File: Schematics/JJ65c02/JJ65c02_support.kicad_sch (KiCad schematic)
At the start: 31 parts, among them SW2 SW_SPDT, U1 74HC00, U2 TXB0108PWR, U3 TXB0104PW, U4 74LS573, U5 TLV2217-33KCSE3, X2 1.8Mhz

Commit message: More work on rp2040-version2
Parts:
- U3: footprint Package_SO:SOIC-14_3.9x8.7mm_P1.27mm -> Package_SO:TSSOP-14_4.4x5mm_P0.65mm
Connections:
- net CLK: now also DECODER1.10 (IN10); no longer DECODER1.1 (CLK/IN1)
- net GND: now also USBC1.B12 (GND)
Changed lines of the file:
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@@
 	)
 	(junction
-		(at 222.25 44.45)
-		(diameter 0)
-		(color 0 0 0 0)
-	)
-	(junction
 		(at 200.66 76.2)
 		(diameter 0)
@@
 		(color 0 0 0 0)
 	)
+	(junction
+		(at 212.09 54.61)
+		(diameter 0)
+		(color 0 0 0 0)
+	)
 	(no_connect
 		(at 39.37 30.48)
@@
 	)
 	(no_connect
+		(at 173.99 76.2)
+	)
+	(no_connect
 		(at 39.37 43.18)
 	)
@@
 	)
 	(no_connect
-		(at 173.99 99.06)
-	)
-	(no_connect
 		(at 234.95 31.75)
 	)
@@
 	(wire
 		(pts
-			(xy 172.72 73.66) (xy 172.72 76.2)
-		)
-		(stroke
-			(width 0)
-			(type default)
-		)
-	)
-	(wire
-		(pts
 			(xy 38.1 185.42) (xy 39.37 185.42)
 		)
@@
 	(wire
 		(pts
+			(xy 212.09 54.61) (xy 222.25 54.61)
+		)
+		(stroke
+			(width 0)
+			(type default)
+		)
+	)
+	(wire
+		(pts
 			(xy 153.67 46.99) (xy 162.56 46.99)
 		)
@@
 	(wire
 		(pts
+			(xy 222.25 44.45) (xy 222.25 54.61)
+		)
+		(stroke
+			(width 0)
+			(type default)
+		)
+	)
+	(wire
+		(pts
 			(xy 232.41 77.47) (xy 229.87 77.47)
 		)
@@
 	(wire
 		(pts
+			(xy 207.01 54.61) (xy 212.09 54.61)
+		)
+		(stroke
+			(width 0)
+			(type default)
+		)
+	)
+	(wire
+		(pts
 			(xy 250.19 72.39) (xy 250.19 74.93)
 		)
@@
 		)
 	)
-	(bus
+	(wire
 		(pts
-			(xy 166.37 76.2) (xy 166.37 78.74)
+			(xy 171.45 99.06) (xy 173.99 99.06)
 		)
 		(stroke
@@
 		)
 	)
-	(wire
+	(bus
 		(pts
-			(xy 171.45 91.44) (xy 173.99 91.44)
+			(xy 166.37 76.2) (xy 166.37 78.74)
 		)
 		(stroke
@@
 	(wire
 		(pts
-			(xy 199.39 99.06) (xy 201.93 99.06)
+			(xy 171.45 91.44) (xy 173.99 91.44)
 		)
 		(stroke
@@
 	(wire
 		(pts
-			(xy 222.25 40.64) (xy 222.25 44.45)
+			(xy 199.39 99.06) (xy 201.93 99.06)
 		)
 		(stroke
@@
 	(wire
 		(pts
-			(xy 171.45 73.66) (xy 172.72 73.66)
-		)
-		(stroke
-			(width 0)
-			(type default)
-		)
-	)
-	(wire
-		(pts
 			(xy 34.29 33.02) (xy 34.29 41.91)
 		)
@@
 	(wire
 		(pts
-			(xy 172.72 76.2) (xy 173.99 76.2)
-		)
-		(stroke
-			(width 0)
-			(type default)
-		)
-	)
-	(wire
-		(pts
 			(xy 157.48 137.16) (xy 157.48 148.59)
 		)
@@
 	(global_label "CLK"
 		(shape input)
-		(at 171.45 73.66 180)
+		(at 171.45 99.06 180)
 		(fields_autoplaced yes)
 		(effects
@@
 		)
 		(property "Intersheetrefs" "${INTERSHEET_REFS}"
-			(at 165.9051 73.66 0)
+			(at 165.9051 99.06 0)
 			(effects
 				(font
@@
 			)
 		)
-		(property "Description" ""
+		(property "Description" "Crystal Clock Oscillator, DIP14-style metal package"
 			(at 120.65 36.83 0)
 			(effects
@@
 			)
 		)
-		(property "Description" ""
+		(property "Description" "Light emitting diode"
 			(at 162.56 40.64 0)
 			(effects
@@
 			)
 		)
-		(property "Description" ""
+		(property "Description" "Resistor"
 			(at 162.56 33.02 0)
 			(effects
@@
 			)
 		)
-		(property "Description" ""
+		(property "Description" "Unpolarized capacitor"
 			(at 125.73 144.78 0)
 			(effects
@@
 			)
 		)
-		(property "Description" ""
+		(property "Description" "Resistor"
 			(at 135.89 144.78 0)
 			(effects
@@
 			)
 		)
-		(property "Description" ""
+		(property "Description" "quad 2-input NAND gate"
 			(at 242.57 74.93 0)
 			(effects
@@
 			)
 		)
-		(property "Description" ""
+		(property "Description" "Resistor"
 			(at 232.41 83.82 0)
 			(effects
@@
 			)
 		)
-		(property "Description" ""
+		(property "Description" "Resistor"
 			(at 24.13 48.26 0)
 			(effects
@@
 			)
 		)
-		(property "Description" ""
+		(property "Description" "Switch, single pole double throw"
 			(at 229.87 29.21 0)
 			(effects
@@
 			)
 		)
-		(property "Description" ""
+		(property "Description" "Resistor"
 			(at 152.4 144.78 0)
 			(effects
@@
 			)
 		)
-		(property "Footprint" "Package_SO:SOIC-14_3.9x8.7mm_P1.27mm"
+		(property "Footprint" "Package_SO:TSSOP-14_4.4x5mm_P0.65mm"
 			(at 124.46 109.22 0)
 			(effects
@@
 			)
 		)
-		(property "Description" ""
+		(property "Description" "4-Bit Bidirectional Voltage-Level Translator, Auto Direction Sensing and ±15-kV ESD Protection, 1.2 - 3.6V APort, 1.65 - 5.5V BPort, TSSOP-14"
 			(at 124.46 90.17 0)
 			(effects
@@
 			)
 		)
-		(property "Description" ""
+		(property "Description" "Audio Jack, 3 Poles (Stereo / TRS)"
 			(at 162.56 151.13 0)
 			(effects
@@
 			)
 		)
-		(property "Description" ""
+		(property "Description" "Resistor"
 			(at 26.67 27.94 0)
 			(effects
@@
 			)
 		)
-		(property "Description" ""
+		(property "Description" "Unpolarized capacitor"
 			(at 72.39 125.73 0)
 			(effects
@@
 			)
 		)
-		(property "Description" ""
+		(property "Description" "6-pin Mini-DIN connector"
 			(at 81.28 54.61 0)
 			(effects
@@
 			)
 		)
-		(property "Description" ""
+		(property "Description" "Polarized capacitor"
 			(at 262.89 39.37 0)
 			(effects
@@
 			)
 		)
-		(property "Description" ""
+		(property "Description" "15-pin female receptacle socket D-SUB connector, High density (3 columns), Triple Row, Generic, VGA-connector"
 			(at 46.99 38.1 0)
 			(effects
@@
 			)
 		)
-		(property "Description" ""
+		(property "Description" "Unpolarized capacitor"
 			(at 196.85 64.77 0)
 			(effects
@@
 			)
 		)
-		(property "Description" ""
+		(property "Description" "Unpolarized capacitor"
 			(at 143.51 153.67 0)
 			(effects
@@
 			)
 		)
-		(property "Description" ""
+		(property "Description" "Resistor"
 			(at 34.29 48.26 0)
 			(effects
@@
 			)
 		)
-		(property "Description" ""
+		(property "Description" "Resistor"
 			(at 29.21 48.26 0)
 			(effects
@@
 			)
 		)
-		(property "Description" ""
+		(property "Description" "Resistor"
 			(at 26.67 38.1 0)
 			(effects
@@
 			)
 		)
-		(property "Description" ""
+		(property "Description" "quad 2-input NAND gate"
 			(at 257.81 74.93 0)
 			(effects
@@
 			)
 		)
-		(property "Description" ""
+		(property "Description" "Resistor"
 			(at 119.38 153.67 0)
 			(effects
@@
 			)
 		)
-		(property "Description" ""
+		(property "Description" "USB Power-Only 6P Type-C Receptacle connector"
 			(at 207.01 36.83 0)
 			(effects
@@
 		(pin "1"
 		)
-		(pin "2"
-		)
 		(pin "3"
 		)
 		(pin "4"
 		)
+		(pin "B12"
+		)
+		(pin "1"
+		)
+		(pin "2"
+		)
 		(instances
 			(project "JJ65c02"
@@
 			)
 		)
-		(property "Description" ""
+		(property "Description" "8-bit Latch 3-state outputs"
 			(at 220.98 133.35 0)
 			(effects
@@
 			)
 		)
-		(property "Description" ""
+		(property "Description" "Resistor"
 			(at 26.67 33.02 0)
 			(effects
@@
 			)
 		)
-		(property "Description" ""
+		(property "Description" "50mA Ultra-Low Quiescent Current LDO Voltage Regulator, 3.3V fixed output, TO-252/SOT-223"
 			(at 250.19 33.02 0)
 			(effects

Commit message: Latest Kicad schematics and PCB
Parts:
- removed R1: 4.7K, Resistor_THT:R_Axial_DIN0207_L6.3mm_D2.5mm_P7.62mm_Horizontal, symbol Device:R
- removed R11, R13, R14: 470, Resistor_THT:R_Axial_DIN0207_L6.3mm_D2.5mm_P7.62mm_Horizontal, symbol Device:R
- removed R15, R16, R17: 1k, Resistor_THT:R_Axial_DIN0207_L6.3mm_D2.5mm_P7.62mm_Horizontal, symbol Device:R
- added RN2: 4.7k, Resistor_THT:R_Array_SIP6, symbol Device:R_Pack03_SIP_Split
- added RN3: 1k, Resistor_THT:R_Array_SIP6, symbol Device:R_Pack03_SIP_Split
- added RN4: 470, Resistor_THT:R_Array_SIP6, symbol Device:R_Pack03_SIP_Split
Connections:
- net +5V: now also RN2.5 (R3.1)
- net A~{IRQ}: now also RN2.6 (R3.2)
- net BLUE: now also RN4.5 (R3.1)
- net BRIGHT: now also RN3.1 (R1.1), RN3.3 (R2.1), RN3.5 (R3.1)
- net GND: no longer USBC1.B12 (GND)
- net GREEN: now also RN4.3 (R2.1)
- net RED: now also RN4.1 (R1.1)
- net at VGA1.1: now also RN3.2 (R1.2), RN4.2 (R1.2)
- net at VGA1.2: now also RN3.4 (R2.2), RN4.4 (R2.2)
- net at VGA1.3: now also RN3.6 (R3.2), RN4.6 (R3.2)

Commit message: More work on rp2040 updates
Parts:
- U3: footprint Package_SO:TSSOP-14_4.4x5mm_P0.65mm -> Package_SO:SOIC-14_3.9x8.7mm_P1.27mm
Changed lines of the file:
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@@
 			)
 		)
-		(property "Footprint" "Package_SO:TSSOP-14_4.4x5mm_P0.65mm"
+		(property "Footprint" "Package_SO:SOIC-14_3.9x8.7mm_P1.27mm"
 			(at 124.46 109.22 0)
 			(effects

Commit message: Latest versions
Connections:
- net CLK: now also DECODER1.1 (CLK/IN1)
- no-connect marks 35 -> 34
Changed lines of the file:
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@@
 (kicad_sch
-	(version 20231120)
+	(version 20250114)
 	(generator "eeschema")
-	(generator_version "8.0")
+	(generator_version "9.0")
 	(paper "A4")
 	(title_block
@@
 		(comment 4 "Support Circuits")
 	)
+	(text "Support Schematics"
+		(exclude_from_sim no)
+		(at 132.08 17.78 0)
+		(effects
+			(font
+				(size 2.4892 2.4892)
+			)
+			(justify left bottom)
+		)
+	)
+	(text "~{IRQ} Logic Glue"
+		(exclude_from_sim no)
+		(at 240.03 87.63 0)
+		(effects
+			(font
+				(size 2.4892 2.4892)
+			)
+			(justify left bottom)
+		)
+	)
 	(junction
 		(at 262.89 33.02)
@@
 	)
 	(no_connect
-		(at 173.99 76.2)
-	)
-	(no_connect
 		(at 39.37 43.18)
 	)
@@
 	(wire
 		(pts
+			(xy 173.99 73.66) (xy 172.72 73.66)
+		)
+		(stroke
+			(width 0)
+			(type default)
+		)
+	)
+	(wire
+		(pts
 			(xy 234.95 72.39) (xy 229.87 72.39)
 		)
@@
 		)
 	)
+	(wire
+		(pts
+			(xy 173.99 76.2) (xy 173.99 73.66)
+		)
+		(stroke
+			(width 0)
+			(type default)
+		)
+	)
 	(bus
 		(pts
@@
 		)
 	)
-	(text "Support Schematics"
-		(exclude_from_sim no)
-		(at 132.08 17.78 0)
-		(effects
-			(font
-				(size 2.4892 2.4892)
-			)
-			(justify left bottom)
-		)
-	)
-	(text "~{IRQ} Logic Glue"
-		(exclude_from_sim no)
-		(at 240.03 87.63 0)
-		(effects
-			(font
-				(size 2.4892 2.4892)
-			)
-			(justify left bottom)
-		)
-	)
 	(label "a11"
 		(at 172.72 88.9 180)
-		(fields_autoplaced yes)
 		(effects
 			(font
@@
 	(label "pa3v0"
 		(at 33.02 134.62 0)
-		(fields_autoplaced yes)
 		(effects
 			(font
@@
 	(label "d0"
 		(at 204.47 120.65 0)
-		(fields_autoplaced yes)
 		(effects
 			(font
@@
 	(label "pa3v2"
 		(at 33.02 88.9 0)
-		(fields_autoplaced yes)
 		(effects
 			(font
@@
 	(label "pa3v6"
 		(at 33.02 99.06 0)
-		(fields_autoplaced yes)
 		(effects
 			(font
@@
 	(label "d1"
 		(at 204.47 123.19 0)
-		(fields_autoplaced yes)
 		(effects
 			(font
@@
 	(label "d3v4"
 		(at 238.76 130.81 180)
-		(fields_autoplaced yes)
 		(effects
 			(font
@@
 	(label "pa3v1"
 		(at 33.02 86.36 0)
-		(fields_autoplaced yes)
 		(effects
 			(font
@@
 	(label "d4"
 		(at 204.47 130.81 0)
-		(fields_autoplaced yes)
 		(effects
 			(font
@@
 	(label "pa3v6"
 		(at 33.02 154.94 0)
-		(fields_autoplaced yes)
 		(effects
 			(font
@@
 	(label "pa3v5"
 		(at 33.02 96.52 0)
-		(fields_autoplaced yes)
 		(effects
 			(font
@@
 	(label "a14"
 		(at 172.72 81.28 180)
-		(fields_autoplaced yes)
 		(effects
 			(font
@@
 	(label "d6"
 		(at 204.47 135.89 0)
-		(fields_autoplaced yes)
 		(effects
 			(font
@@
 	(label "pa1"
 		(at 73.66 86.36 0)
-		(fields_autoplaced yes)
 		(effects
 			(font
@@
 	(label "d3v3"
 		(at 35.56 167.64 0)
-		(fields_autoplaced yes)
 		(effects
 			(font
@@
 	(label "d7"
 		(at 204.47 138.43 0)
-		(fields_autoplaced yes)
 		(effects
 			(font
@@
 	(label "a12"
 		(at 172.72 86.36 180)
-		(fields_autoplaced yes)
 		(effects
 			(font
@@
 	(label "a13"
 		(at 172.72 83.82 180)
-		(fields_autoplaced yes)
 		(effects
 			(font
@@
 	(label "pa3v2"
 		(at 33.02 142.24 0)
-		(fields_autoplaced yes)
 		(effects
 			(font
@@
 	(label "d3v7"
 		(at 35.56 180.34 0)
-		(fields_autoplaced yes)
 		(effects
 			(font
@@
 	(label "d3v1"
 		(at 238.76 123.19 180)
-		(fields_autoplaced yes)
 		(effects
 			(font
@@
 	(label "pa3v3"
 		(at 33.02 91.44 0)
-		(fields_autoplaced yes)
 		(effects
 			(font
@@
 	(label "d3v5"
 		(at 238.76 133.35 180)
-		(fields_autoplaced yes)
 		(effects
 			(font
@@
 	(label "d3v0"
 		(at 238.76 120.65 180)
-		(fields_autoplaced yes)
 		(effects
 			(font
@@
 	(label "pa3v0"
 		(at 33.02 83.82 0)
-		(fields_autoplaced yes)
 		(effects
 			(font
@@
 	(label "pa3"
 		(at 73.66 91.44 0)
-		(fields_autoplaced yes)
 		(effects
 			(font
@@
 	(label "d3v2"
 		(at 35.56 162.56 0)
-		(fields_autoplaced yes)
 		(effects
 			(font
@@
 	(label "pa3v1"
 		(at 33.02 137.16 0)
-		(fields_autoplaced yes)
 		(effects
 			(font
@@
 	(label "pa4"
 		(at 73.66 93.98 0)
-		(fields_autoplaced yes)
 		(effects
 			(font
@@
 	(label "pa3v4"
 		(at 33.02 147.32 0)
-		(fields_autoplaced yes)
 		(effects
 			(font
@@
 	(label "d5"
 		(at 204.47 133.35 0)
-		(fields_autoplaced yes)
 		(effects
 			(font
@@
 	(label "pa0"
 		(at 73.66 83.82 0)
-		(fields_autoplaced yes)
 		(effects
 			(font
@@
 	(label "d3v5"
 		(at 35.56 172.72 0)
-		(fields_autoplaced yes)
 		(effects
 			(font
@@
 	(label "pa5"
 		(at 73.66 96.52 0)
-		(fields_autoplaced yes)
 		(effects
 			(font
@@
 	(label "d3v1"
 		(at 35.56 160.02 0)
-		(fields_autoplaced yes)
 		(effects
 			(font
@@
 	(label "a15"
 		(at 172.72 78.74 180)
-		(fields_autoplaced yes)
 		(effects
 			(font
@@
 	(label "pa6"
 		(at 73.66 99.06 0)
-		(fields_autoplaced yes)
 		(effects
 			(font
@@
 	(label "d3v6"
 		(at 238.76 135.89 180)
-		(fields_autoplaced yes)
 		(effects
 			(font
@@
 	(label "d3v4"
 		(at 35.56 170.18 0)
-		(fields_autoplaced yes)
 		(effects
 			(font
@@
 	(label "d3v3"
 		(at 238.76 128.27 180)
-		(fields_autoplaced yes)
 		(effects
 			(font
@@
 	(label "d3v7"
 		(at 238.76 138.43 180)
-		(fields_autoplaced yes)
 		(effects
 			(font
@@
 	(label "pa3v4"
 		(at 33.02 93.98 0)
-		(fields_autoplaced yes)
 		(effects
 			(font
@@
 	(label "pa2"
 		(at 73.66 88.9 0)
-		(fields_autoplaced yes)
 		(effects
 			(font
@@
 	(label "d2"
 		(at 204.47 125.73 0)
-		(fields_autoplaced yes)
 		(effects
 			(font
@@
 	(label "pa3v3"
 		(at 33.02 144.78 0)
-		(fields_autoplaced yes)
 		(effects
 			(font
@@
 	(label "d3"
 		(at 204.47 128.27 0)
-		(fields_autoplaced yes)
 		(effects
 			(font
@@
 	(label "d3v2"
 		(at 238.76 125.73 180)
-		(fields_autoplaced yes)
 		(effects
 			(font
@@
 	(label "pa3v5"
 		(at 33.02 149.86 0)
-		(fields_autoplaced yes)
 		(effects
 			(font
@@
 	(label "d3v6"
 		(at 35.56 175.26 0)
-		(fields_autoplaced yes)
 		(effects
 			(font
@@
 	(label "d3v0"
 		(at 35.56 157.48 0)
-		(fields_autoplaced yes)
 		(effects
 			(font
@@
 			(effects
 				(font
+					(size 1.27 1.27)
+				)
+				(justify right)
+				(hide yes)
+			)
+		)
+	)
+	(global_label "CLK"
+		(shape input)
+		(at 172.72 73.66 180)
+		(fields_autoplaced yes)
+		(effects
+			(font
+				(size 1.1938 1.1938)
+			)
+			(justify right)
+		)
+		(property "Intersheetrefs" "${INTERSHEET_REFS}"
+			(at 167.1751 73.66 0)
+			(effects
+				(font

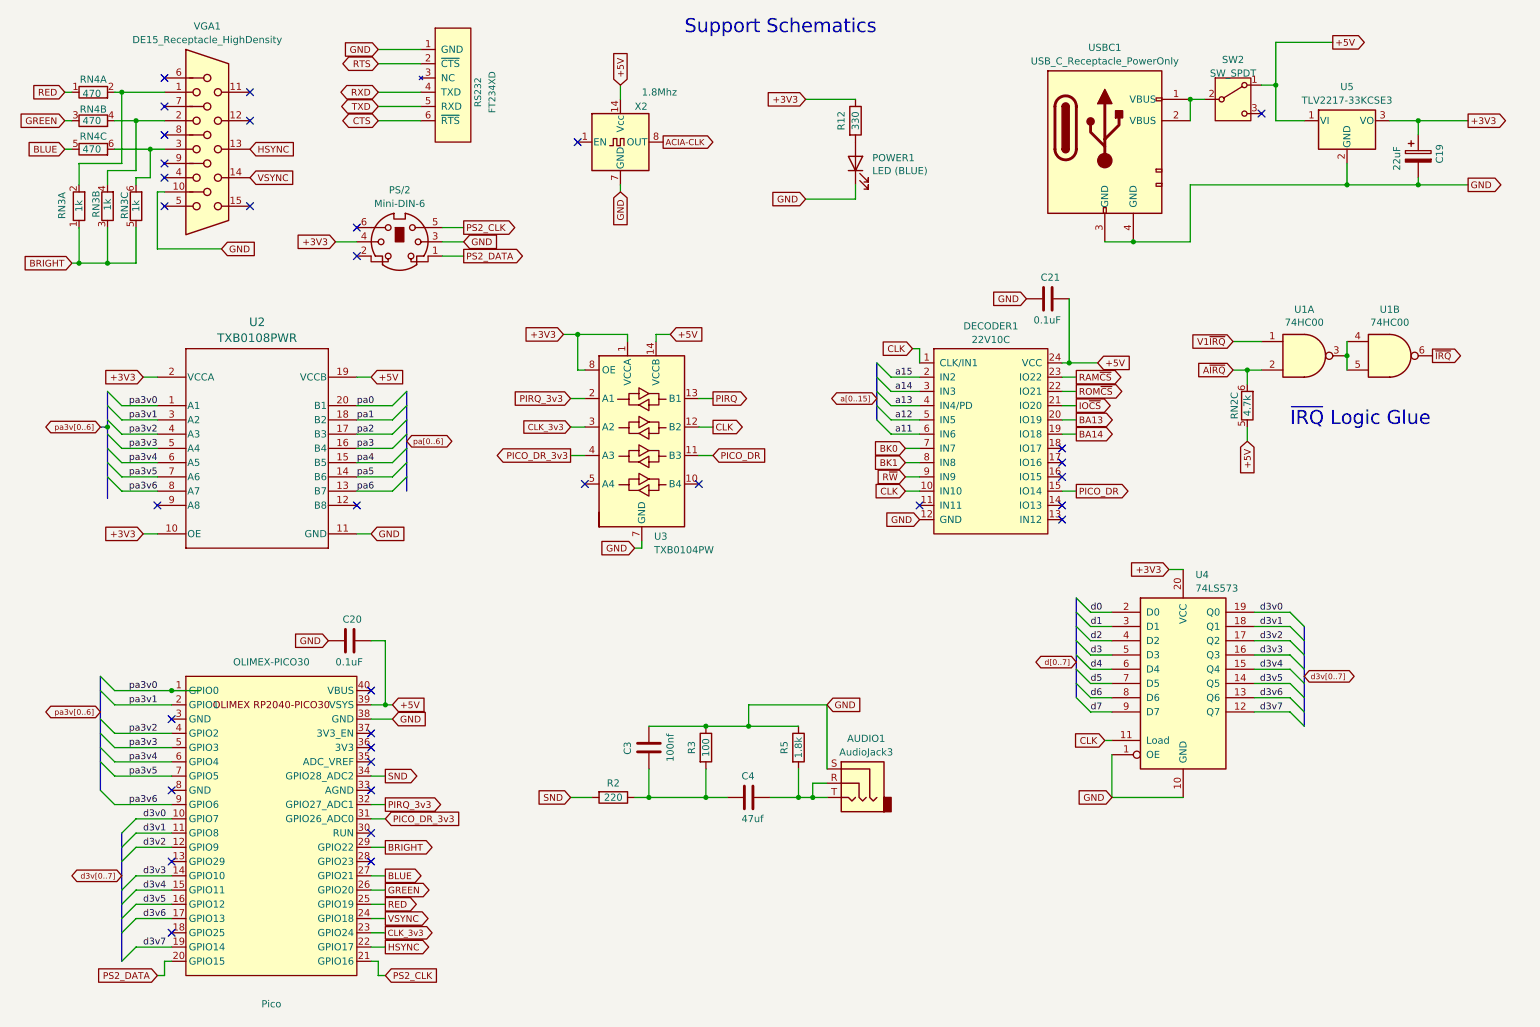
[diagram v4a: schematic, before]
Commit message: No longer use pi pico for sys clk generation - not enough pins on standard Pico board
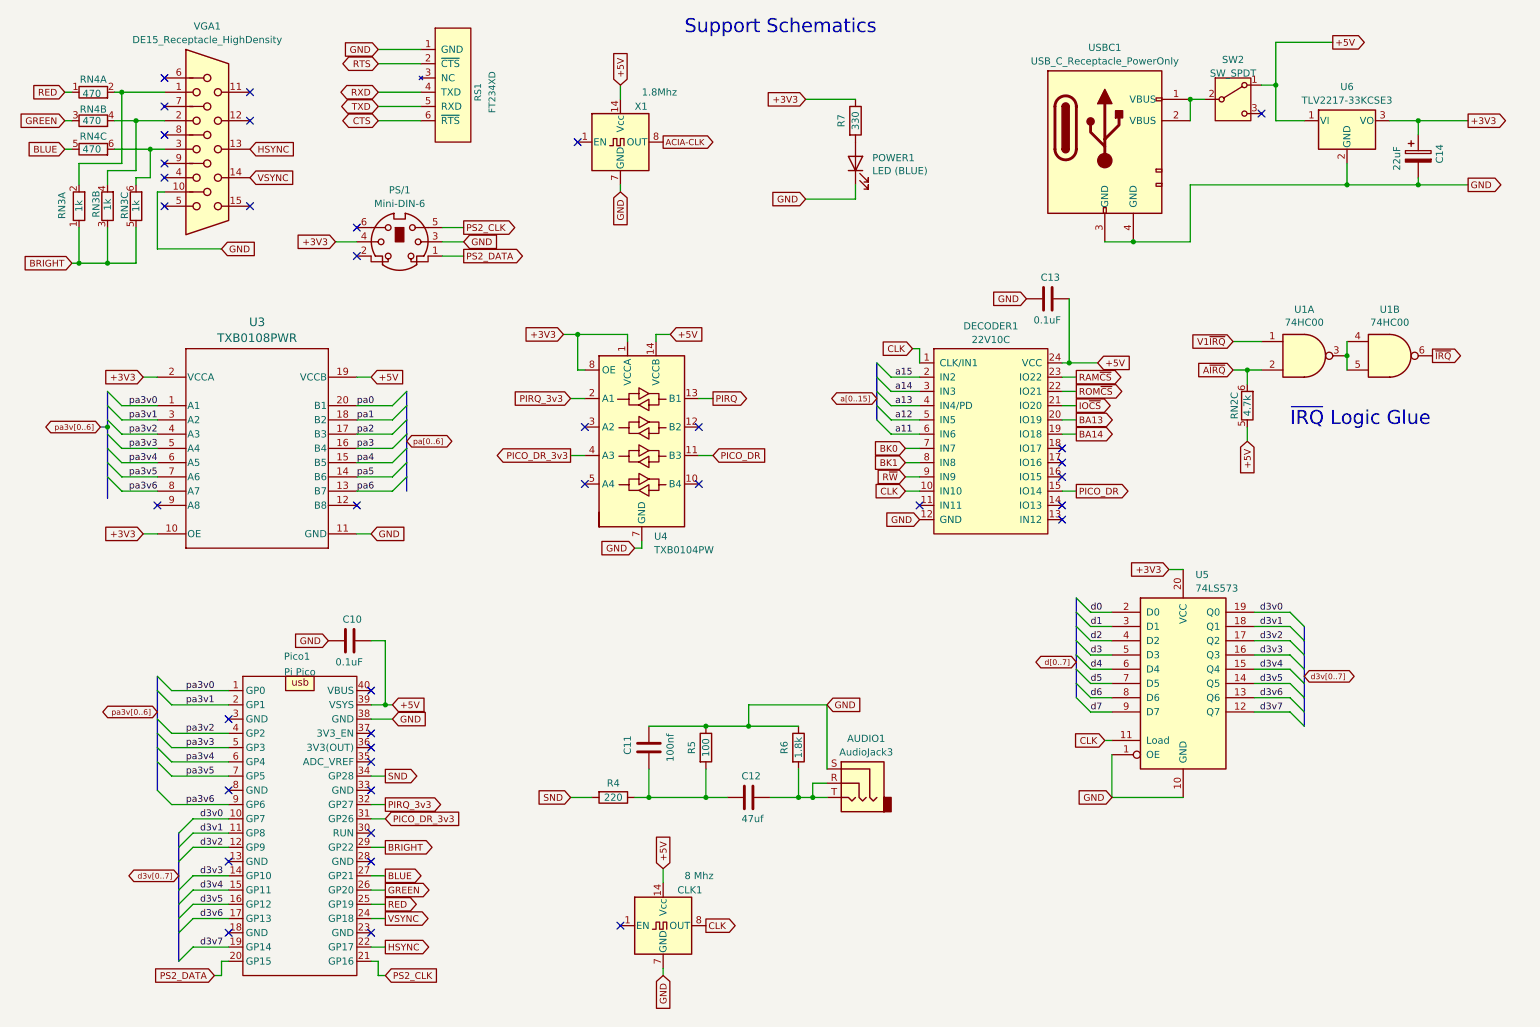
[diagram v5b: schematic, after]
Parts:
- removed OLIMEX-PICO30: Pico, JJ65c02:RPi_Pico_SMD_TH, symbol JJ65c02-rescue:Pico
- added CLK1: 8 Mhz, Oscillator:Oscillator_DIP-14, symbol Oscillator:CXO_DIP14
- added Pico1: Pi Pico, Library:Raspberry_pi_pico, symbol JJ65c02-rescue:pi_pico
- renumbered C20 to C10, C3 to C11, C4 to C12, C21 to C13, C19 to C14, PS/2 to PS/1, R2 to R4, R3 to R5, R5 to R6, R12 to R7, RS232 to RS1, U2 to U3, U3 to U4, U4 to U5, U5 to U6, X2 to X1
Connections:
- net +5V: now also CLK1.14 (Vcc), Pico1.39 (VSYS)
- net BLUE: now also Pico1.27 (GP21)
- net BRIGHT: now also Pico1.29 (GP22)
- net CLK: now also CLK1.8 (OUT); no longer U4.12 (B2)
- net GND: now also CLK1.7 (GND), Pico1.38 (GND)
- net GREEN: now also Pico1.26 (GP20)
- net HSYNC: now also Pico1.22 (GP17)
- net PICO_DR_3v3: now also Pico1.31 (GP26)
- net PIRQ_3v3: now also Pico1.32 (GP27)
- net PS2_CLK: now also Pico1.21 (GP16)
- net PS2_DATA: now also Pico1.20 (GP15)
- net RED: now also Pico1.25 (GP19)
- net SND: now also Pico1.34 (GP28)
- net VSYNC: now also Pico1.24 (GP18)
- net d3v0: now also Pico1.10 (GP7)
- net d3v1: now also Pico1.11 (GP8)
- net d3v2: now also Pico1.12 (GP9)
- net d3v3: now also Pico1.14 (GP10)
- net d3v4: now also Pico1.15 (GP11)
- net d3v5: now also Pico1.16 (GP12)
- net d3v6: now also Pico1.17 (GP13)
- net d3v7: now also Pico1.19 (GP14)
- net pa3v0: now also Pico1.1 (GP0)
- net pa3v1: now also Pico1.2 (GP1)
- net pa3v2: now also Pico1.4 (GP2)
- net pa3v3: now also Pico1.5 (GP3)
- net pa3v4: now also Pico1.6 (GP4)
- net pa3v5: now also Pico1.7 (GP5)
- net pa3v6: now also Pico1.9 (GP6)
- net CLK_3v3: no longer names the net of U4.3 (A2)
- no-connect marks 34 -> 38

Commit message: Updates
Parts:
- R6: value 1.8k -> 2k
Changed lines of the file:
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@@
 			)
 		)
-		(property "Value" "1.8k"
+		(property "Value" "2k"
 			(at 152.4 144.78 90)
 			(effects
@@
 			)
 		)
-		(property "Datasheet" " ~"
+		(property "Datasheet" "~"
 			(at 22.86 27.94 0)
 			(effects
